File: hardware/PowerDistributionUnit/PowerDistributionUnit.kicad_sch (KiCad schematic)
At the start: 96 parts, among them J1 973582101, J2 973582100, J3 973582101, J4 973582100, Q1 SQJ141ELP, Q2 CSD18511Q5A, SW1 SW_Push, U1 TPS25983, U2 AD5258, U3 NUCLEO_L432KC

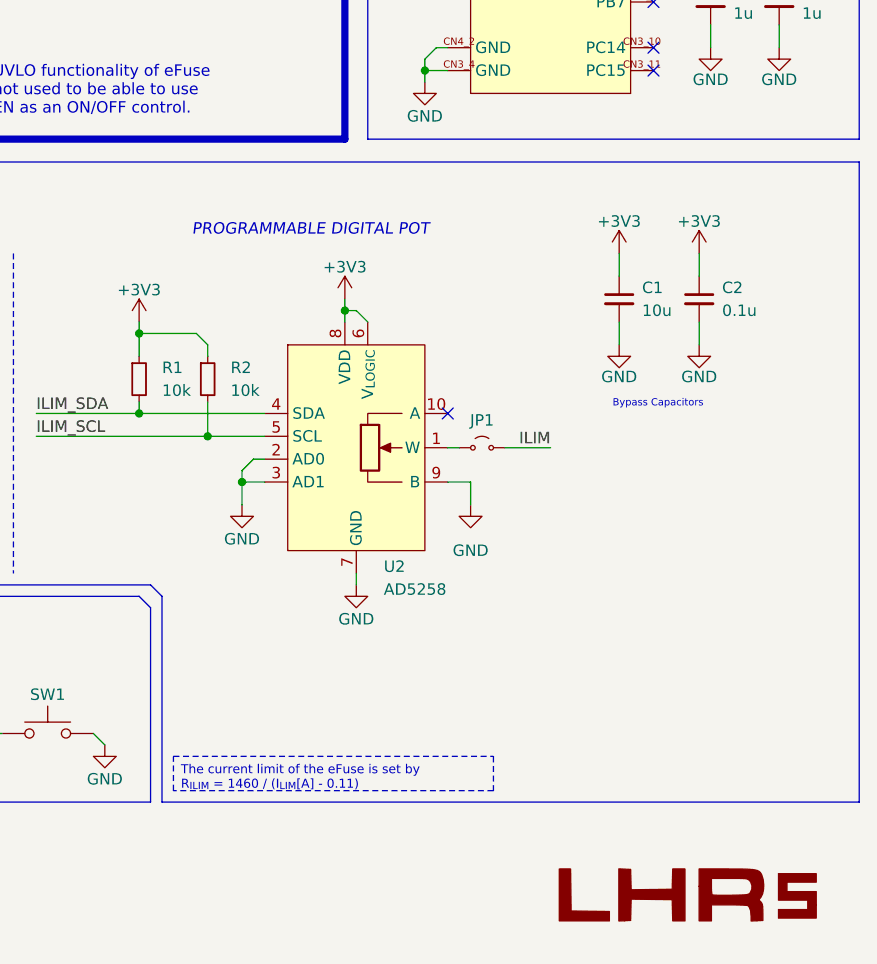
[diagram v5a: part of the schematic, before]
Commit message: added mounting holes
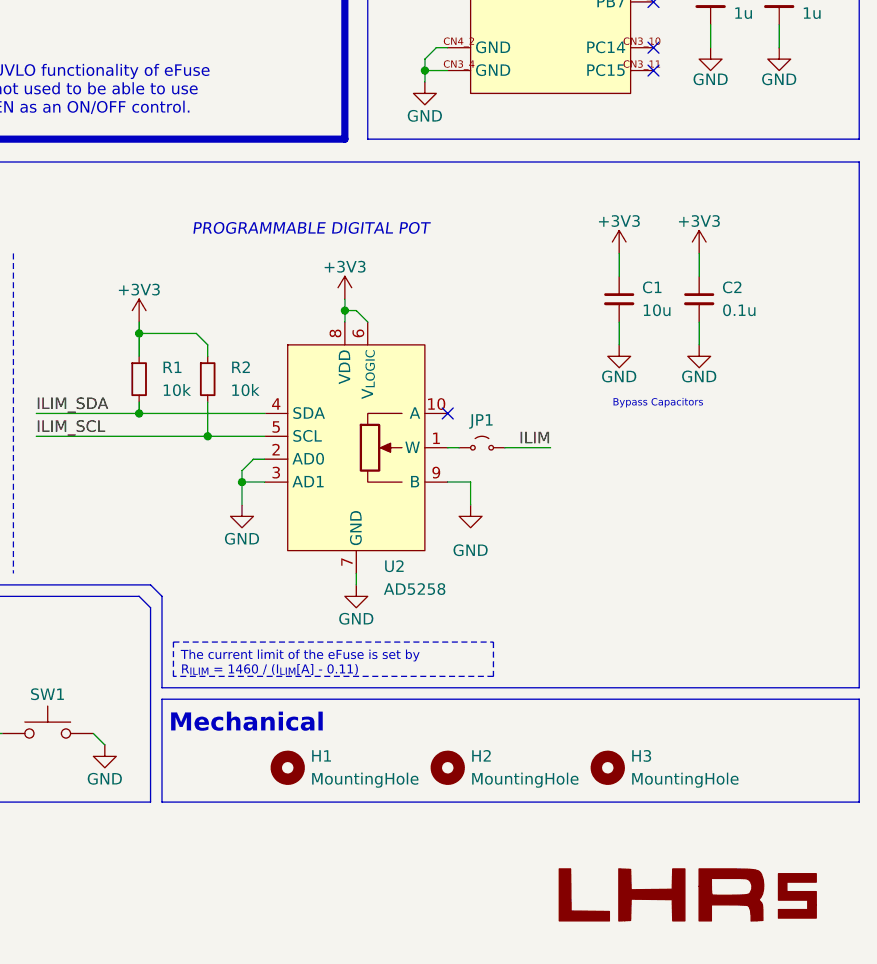
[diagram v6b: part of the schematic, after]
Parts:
- added H1, H2, H3: MountingHole, MountingHole:MountingHole_3.2mm_M3, symbol Mechanical:MountingHole
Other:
- note added: "Mechanical"
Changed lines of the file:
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@@
 	(polyline
 		(pts
-			(xy 280.67 92.71) (xy 280.67 163.83)
+			(xy 280.67 92.71) (xy 280.67 151.13)
 		)
 		(stroke
@@
 	(polyline
 		(pts
-			(xy 203.2 140.97) (xy 203.2 163.83)
+			(xy 203.2 140.97) (xy 203.2 151.13)
 		)
 		(stroke
@@
 	(polyline
 		(pts
-			(xy 203.2 163.83) (xy 280.67 163.83)
+			(xy 203.2 151.13) (xy 280.67 151.13)
 		)
 		(stroke
@@
 	)
 	(rectangle
+		(start 203.2 152.4)
+		(end 280.67 163.83)
+		(stroke
+			(width 0)
+			(type default)
+		)
+		(fill
+			(type none)
+		)
+	)
+	(rectangle
 		(start 16.51 92.71)
 		(end 53.34 132.08)
@@
 	(text_box "The current limit of the eFuse is set by\nR_{ILIM} = 1460 / (I_{LIM}[A] - 0.11)\n\n"
 		(exclude_from_sim no)
-		(at 204.47 158.75 0)
+		(at 204.47 146.05 0)
 		(size 35.56 3.81)
 		(stroke
@@
 		)
 	)
+	(text "Mechanical"
+		(exclude_from_sim no)
+		(at 203.962 155.194 0)
+		(effects
+			(font
+				(size 2 2)
+				(thickness 0.254)
+				(bold yes)
+			)
+			(justify left)
+		)
+	)
 	(text "(4 - OPEN)"
 		(exclude_from_sim no)
@@
 	)
 	(symbol
+		(lib_id "Mechanical:MountingHole")
+		(at 252.73 160.02 0)
+		(unit 1)
+		(exclude_from_sim yes)
+		(in_bom no)
+		(on_board yes)
+		(dnp no)
+		(fields_autoplaced yes)
+		(property "Reference" "H3"
+			(at 255.27 158.7499 0)
+			(effects
+				(font
+					(size 1.27 1.27)
+				)
+				(justify left)
+			)
+		)
+		(property "Value" "MountingHole"
+			(at 255.27 161.2899 0)
+			(effects
+				(font
+					(size 1.27 1.27)
+				)
+				(justify left)
+			)
+		)
+		(property "Footprint" "MountingHole:MountingHole_3.2mm_M3"
+			(at 252.73 160.02 0)
+			(effects
+				(font
+					(size 1.27 1.27)
+				)
+				(hide yes)
+			)
+		)
+		(property "Datasheet" "~"
+			(at 252.73 160.02 0)
+			(effects
+				(font
+					(size 1.27 1.27)
+				)
+				(hide yes)
+			)
+		)
+		(property "Description" "Mounting Hole without connection"
+			(at 252.73 160.02 0)
+			(effects
+				(font
+					(size 1.27 1.27)
+				)
+				(hide yes)
+			)
+		)
+		(instances
+			(project "PowerDistributionUnit"
+				(path "/93fa4ef0-f02c-4535-aca9-c62461ff58dd"
+					(reference "H3")
+					(unit 1)
+				)
+			)
+		)
+	)
+	(symbol
 		(lib_id "power:GND")
 		(at 78.74 162.56 0)
@@
 	)
 	(symbol
+		(lib_id "Mechanical:MountingHole")
+		(at 217.17 160.02 0)
+		(unit 1)
+		(exclude_from_sim yes)
+		(in_bom no)
+		(on_board yes)
+		(dnp no)
+		(fields_autoplaced yes)
+		(property "Reference" "H1"
+			(at 219.71 158.7499 0)
+			(effects
+				(font
+					(size 1.27 1.27)
+				)
+				(justify left)
+			)
+		)
+		(property "Value" "MountingHole"
+			(at 219.71 161.2899 0)
+			(effects
+				(font
+					(size 1.27 1.27)
+				)
+				(justify left)
+			)
+		)
+		(property "Footprint" "MountingHole:MountingHole_3.2mm_M3"
+			(at 217.17 160.02 0)
+			(effects
+				(font
+					(size 1.27 1.27)
+				)
+				(hide yes)
+			)
+		)
+		(property "Datasheet" "~"
+			(at 217.17 160.02 0)
+			(effects
+				(font
+					(size 1.27 1.27)
+				)
+				(hide yes)
+			)
+		)
+		(property "Description" "Mounting Hole without connection"
+			(at 217.17 160.02 0)
+			(effects
+				(font
+					(size 1.27 1.27)
+				)
+				(hide yes)
+			)
+		)
+		(instances
+			(project ""
+				(path "/93fa4ef0-f02c-4535-aca9-c62461ff58dd"
+					(reference "H1")
+					(unit 1)
+				)
+			)
+		)
+	)
+	(symbol
 		(lib_id "power:GND")
 		(at 196.85 157.48 0)
@@
 					(unit 1)
 				)
+			)
+		)
+	)
+	(symbol
+		(lib_id "Mechanical:MountingHole")
+		(at 234.95 160.02 0)
+		(unit 1)
+		(exclude_from_sim yes)
+		(in_bom no)
+		(on_board yes)
+		(dnp no)
+		(fields_autoplaced yes)
+		(property "Reference" "H2"
+			(at 237.49 158.7499 0)
+			(effects
+				(font
+					(size 1.27 1.27)
+				)
+				(justify left)
+			)
+		)
+		(property "Value" "MountingHole"
+			(at 237.49 161.2899 0)
+			(effects
+				(font
+					(size 1.27 1.27)
+				)
+				(justify left)
+			)
+		)
+		(property "Footprint" "MountingHole:MountingHole_3.2mm_M3"
+			(at 234.95 160.02 0)
+			(effects
+				(font
+					(size 1.27 1.27)
+				)
+				(hide yes)
+			)
+		)
+		(property "Datasheet" "~"
+			(at 234.95 160.02 0)
+			(effects
+				(font
+					(size 1.27 1.27)
+				)
+				(hide yes)
+			)
+		)
+		(property "Description" "Mounting Hole without connection"
+			(at 234.95 160.02 0)
+			(effects
+				(font
+					(size 1.27 1.27)
+				)
+				(hide yes)
+			)
+		)
+		(instances
+			(project "PowerDistributionUnit"
+				(path "/93fa4ef0-f02c-4535-aca9-c62461ff58dd"
+					(reference "H2")
+					(unit 1)
+				)

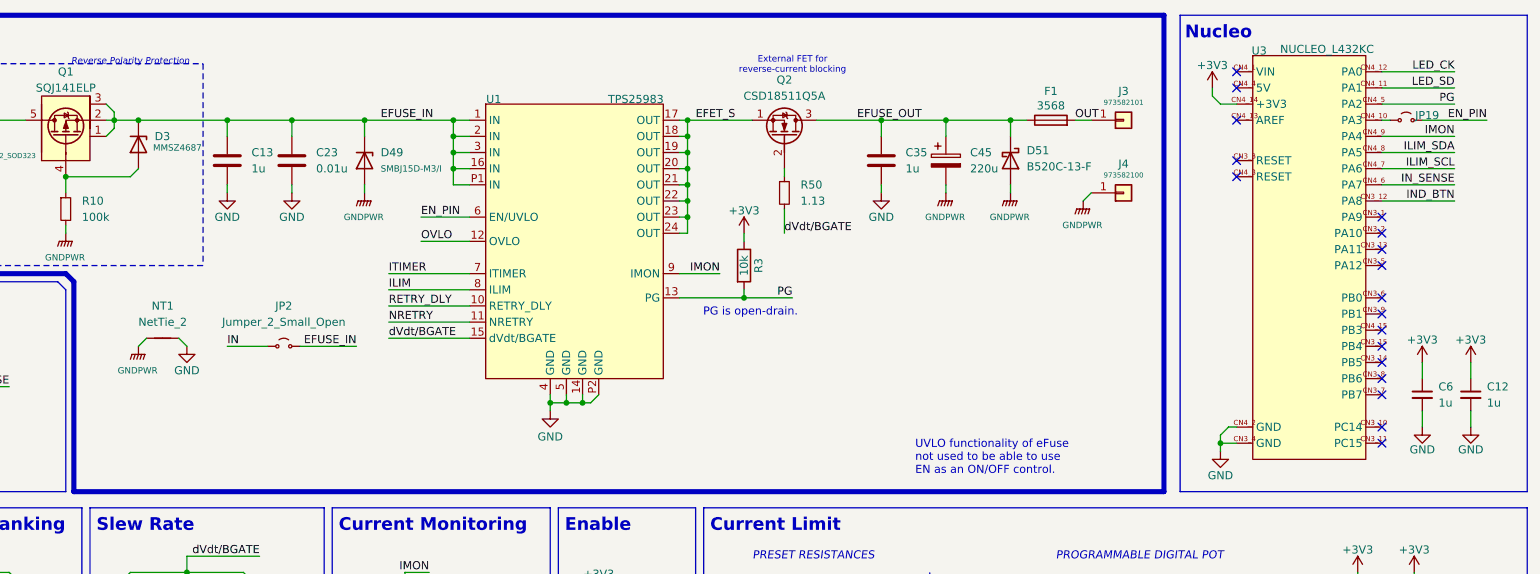
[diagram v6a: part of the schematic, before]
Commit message: added pours, traces, & labels, revised courtyard around TPS25983 footprint, added another net tie, ...
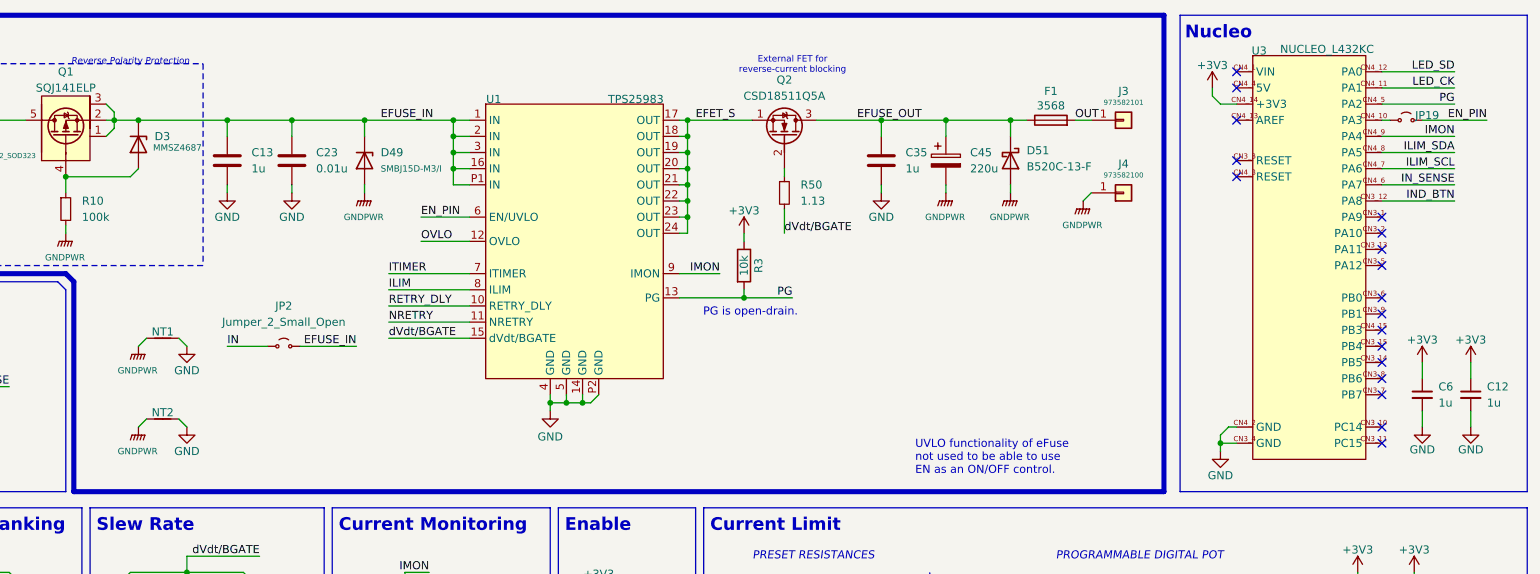
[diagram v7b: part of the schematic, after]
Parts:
- added NT2: NetTie_2, NetTie:NetTie-2_SMD_Pad0.5mm, symbol Device:NetTie_2
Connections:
- net GND: now also NT2.2
- net GNDPWR: now also NT2.1
- net LED_CK: now also U3.CN4_11 (PA1); no longer U3.CN4_12 (PA0)
- net LED_SD: now also U3.CN4_12 (PA0); no longer U3.CN4_11 (PA1)
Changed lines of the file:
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@@
 	(wire
 		(pts
+			(xy 69.85 80.01) (xy 68.58 78.74)
+		)
+		(stroke
+			(width 0)
+			(type default)
+		)
+	)
+	(wire
+		(pts
 			(xy 29.21 72.39) (xy 29.21 73.66)
 		)
@@
 	(wire
 		(pts
-			(xy 257.81 24.13) (xy 269.24 24.13)
-		)
-		(stroke
-			(width 0)
-			(type default)
-		)
-	)
-	(wire
-		(pts
 			(xy 200.66 120.65) (xy 214.63 120.65)
 		)
@@
 	(wire
 		(pts
-			(xy 257.81 26.67) (xy 269.24 26.67)
+			(xy 68.58 191.77) (xy 60.96 191.77)
 		)
 		(stroke
@@
 	(wire
 		(pts
-			(xy 68.58 191.77) (xy 60.96 191.77)
+			(xy 163.83 40.64) (xy 163.83 39.37)
 		)
 		(stroke
@@
 	(wire
 		(pts
-			(xy 163.83 40.64) (xy 163.83 39.37)
+			(xy 223.52 109.22) (xy 224.79 109.22)
 		)
 		(stroke
@@
 	(wire
 		(pts
-			(xy 223.52 109.22) (xy 224.79 109.22)
+			(xy 41.91 102.87) (xy 43.18 104.14)
 		)
 		(stroke
@@
 	(wire
 		(pts
-			(xy 41.91 102.87) (xy 43.18 104.14)
+			(xy 33.02 121.92) (xy 33.02 120.65)
 		)
 		(stroke
@@
 	(wire
 		(pts
-			(xy 33.02 121.92) (xy 33.02 120.65)
+			(xy 80.01 104.14) (xy 80.01 106.68)
 		)
 		(stroke
@@
 	(wire
 		(pts
-			(xy 80.01 104.14) (xy 80.01 106.68)
+			(xy 257.81 26.67) (xy 269.24 26.67)
 		)
 		(stroke
@@
 	(wire
 		(pts
+			(xy 257.81 24.13) (xy 269.24 24.13)
+		)
+		(stroke
+			(width 0)
+			(type default)
+		)
+	)
+	(wire
+		(pts
 			(xy 60.96 120.65) (xy 69.85 120.65)
 		)
@@
 	(wire
 		(pts
+			(xy 62.23 80.01) (xy 63.5 78.74)
+		)
+		(stroke
+			(width 0)
+			(type default)
+		)
+	)
+	(wire
+		(pts
 			(xy 54.61 185.42) (xy 58.42 185.42)
 		)
@@
 	)
 	(label "LED_CK"
-		(at 269.24 24.13 180)
+		(at 269.24 26.67 180)
 		(fields_autoplaced yes)
 		(effects
@@
 	)
 	(label "LED_SD"
-		(at 269.24 26.67 180)
+		(at 269.24 24.13 180)
 		(fields_autoplaced yes)
 		(effects
@@
 		(on_board yes)
 		(dnp no)
-		(fields_autoplaced yes)
 		(property "Reference" "NT1"
-			(at 66.04 60.96 0)
+			(at 66.04 65.024 0)
 			(effects
 				(font
@@
 					(size 1.27 1.27)
 				)
+				(hide yes)
 			)
 		)
@@
 	)
 	(symbol
+		(lib_id "power:GND")
+		(at 69.85 80.01 0)
+		(unit 1)
+		(exclude_from_sim no)
+		(in_bom yes)
+		(on_board yes)
+		(dnp no)
+		(property "Reference" "#PWR025"
+			(at 69.85 86.36 0)
+			(effects
+				(font
+					(size 1.27 1.27)
+				)
+				(hide yes)
+			)
+		)
+		(property "Value" "GND"
+			(at 69.85 83.82 0)
+			(effects
+				(font
+					(size 1.27 1.27)
+				)
+			)
+		)
+		(property "Footprint" ""
+			(at 69.85 80.01 0)
+			(effects
+				(font
+					(size 1.27 1.27)
+				)
+				(hide yes)
+			)
+		)
+		(property "Datasheet" ""
+			(at 69.85 80.01 0)
+			(effects
+				(font
+					(size 1.27 1.27)
+				)
+				(hide yes)
+			)
+		)
+		(property "Description" "Power symbol creates a global label with name \"GND\" , ground"
+			(at 69.85 80.01 0)
+			(effects
+				(font
+					(size 1.27 1.27)
+				)
+				(hide yes)
+			)
+		)
+		(pin "1"
+		)
+		(instances
+			(project "PowerDistributionUnit"
+				(path "/93fa4ef0-f02c-4535-aca9-c62461ff58dd"
+					(reference "#PWR025")
+					(unit 1)
+				)
+			)
+		)
+	)
+	(symbol
 		(lib_id "power:GNDPWR")
 		(at 29.21 83.82 0)
@@
 	)
 	(symbol
+		(lib_id "power:GNDPWR")
+		(at 62.23 80.01 0)
+		(unit 1)
+		(exclude_from_sim no)
+		(in_bom yes)
+		(on_board yes)
+		(dnp no)
+		(property "Reference" "#PWR024"
+			(at 62.23 85.09 0)
+			(effects
+				(font
+					(size 1.27 1.27)
+				)
+				(hide yes)
+			)
+		)
+		(property "Value" "GNDPWR"
+			(at 62.103 83.82 0)
+			(effects
+				(font
+					(size 1 1)
+				)
+			)
+		)
+		(property "Footprint" ""
+			(at 62.23 81.28 0)
+			(effects
+				(font
+					(size 1.27 1.27)
+				)
+				(hide yes)
+			)
+		)
+		(property "Datasheet" ""
+			(at 62.23 81.28 0)
+			(effects
+				(font
+					(size 1.27 1.27)
+				)
+				(hide yes)
+			)
+		)
+		(property "Description" "Power symbol creates a global label with name \"GNDPWR\" , global ground"
+			(at 62.23 80.01 0)
+			(effects
+				(font
+					(size 1.27 1.27)
+				)
+				(hide yes)
+			)
+		)
+		(pin "1"
+		)
+		(instances
+			(project "PowerDistributionUnit"
+				(path "/93fa4ef0-f02c-4535-aca9-c62461ff58dd"
+					(reference "#PWR024")
+					(unit 1)
+				)
+			)
+		)
+	)
+	(symbol
 		(lib_id "Device:D_Zener")
 		(at 97.79 38.1 270)
@@
 					(unit 1)
 				)
+			)
+		)
+	)
+	(symbol
+		(lib_id "Device:NetTie_2")
+		(at 66.04 78.74 0)
+		(unit 1)
+		(exclude_from_sim no)
+		(in_bom no)
+		(on_board yes)
+		(dnp no)
+		(property "Reference" "NT2"
+			(at 66.04 77.724 0)
+			(effects
+				(font
+					(size 1.27 1.27)
+				)
+			)
+		)
+		(property "Value" "NetTie_2"
+			(at 66.04 76.2 0)
+			(effects
+				(font
+					(size 1.27 1.27)
+				)
+				(hide yes)
+			)
+		)
+		(property "Footprint" "NetTie:NetTie-2_SMD_Pad0.5mm"
+			(at 66.04 78.74 0)
+			(effects
+				(font
+					(size 1.27 1.27)
+				)
+				(hide yes)
+			)
+		)
+		(property "Datasheet" "~"
+			(at 66.04 78.74 0)
+			(effects
+				(font
+					(size 1.27 1.27)
+				)
+				(hide yes)
+			)
+		)
+		(property "Description" "Net tie, 2 pins"
+			(at 66.04 78.74 0)
+			(effects
+				(font
+					(size 1.27 1.27)
+				)
+				(hide yes)
+			)
+		)
+		(pin "2"
+		)
+		(pin "1"
+		)
+		(instances
+			(project "PowerDistributionUnit"
+				(path "/93fa4ef0-f02c-4535-aca9-c62461ff58dd"
+					(reference "NT2")
+					(unit 1)
+				)
